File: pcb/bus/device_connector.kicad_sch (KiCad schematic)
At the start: 3 parts, among them J201 Conn_02x10_Row_Letter_First

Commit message: update bus pcb
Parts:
- removed H201, H202: MountingHole_Pad, MountingHole:MountingHole_3.2mm_M3_Pad_Via, symbol Mechanical:MountingHole_Pad
- removed J201: Conn_02x10_Row_Letter_First, PRJ:PCN10-20P-2.54DSA, symbol Connector_Generic:Conn_02x10_Row_Letter_First
- added H401, H402: MountingHole_Pad, MountingHole:MountingHole_3.2mm_M3_Pad_Via, symbol Mechanical:MountingHole_Pad
- added J701: Conn_02x10_Row_Letter_First, PRJ:PCN10-20P-2.54DSA, symbol Connector_Generic:Conn_02x10_Row_Letter_First
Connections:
- net +12V: now also J701.a10 (Pin_a10), J701.a9 (Pin_a9), J701.b10 (Pin_b10), J701.b9 (Pin_b9)
- net +5V: now also J701.a6 (Pin_a6), J701.a7 (Pin_a7), J701.b6 (Pin_b6), J701.b7 (Pin_b7)
- net GND: now also H401.1, H402.1, J701.a1 (Pin_a1), J701.a8 (Pin_a8), J701.b1 (Pin_b1), J701.b8 (Pin_b8)
- net USB+: now also J701.a5 (Pin_a5)
- net USB-: now also J701.b5 (Pin_b5)
- no-connect marks 4 -> 6
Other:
- title: Bus Connector -> (none)

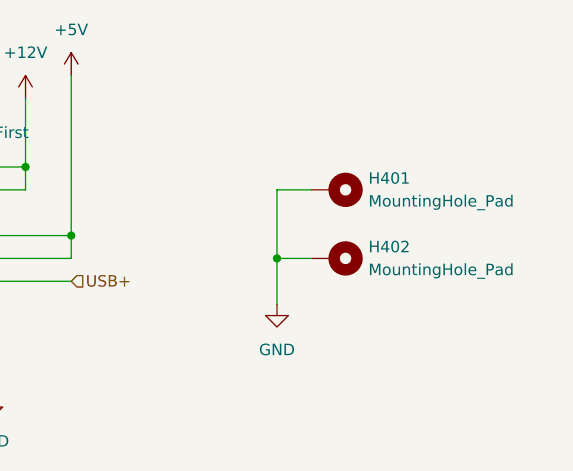
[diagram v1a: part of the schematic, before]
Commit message: update pcb size
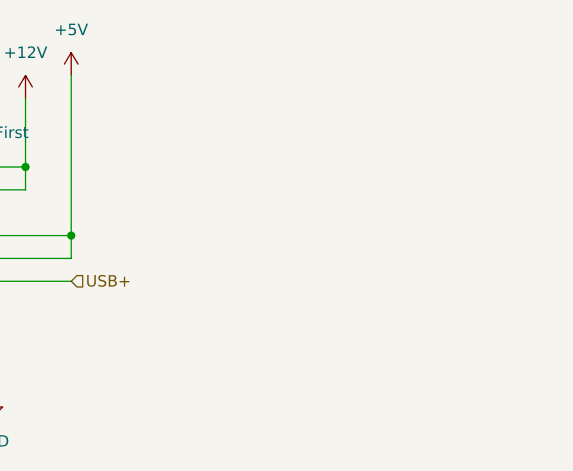
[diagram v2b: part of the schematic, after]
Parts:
- removed H401, H402: MountingHole_Pad, MountingHole:MountingHole_3.2mm_M3_Pad_Via, symbol Mechanical:MountingHole_Pad

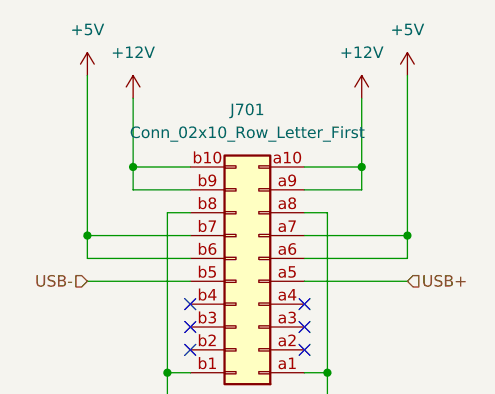
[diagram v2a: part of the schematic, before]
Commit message: upgrade to kicad 9.0.0
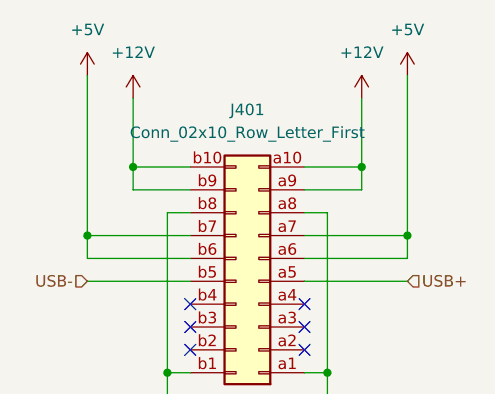
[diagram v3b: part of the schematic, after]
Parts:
- renumbered J701 to J401
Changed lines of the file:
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@@
 (kicad_sch
-	(version 20231120)
+	(version 20250114)
 	(generator "eeschema")
-	(generator_version "8.0")
+	(generator_version "9.0")
 	(paper "A4")
 	(title_block
@@
 		(dnp no)
 		(fields_autoplaced yes)
-		(property "Reference" "#PWR0705"
+		(property "Reference" "#PWR0405"
 			(at 162.56 69.85 0)
 			(effects
@@
 		(dnp no)
 		(fields_autoplaced yes)
-		(property "Reference" "#PWR0703"
+		(property "Reference" "#PWR0403"
 			(at 140.97 105.41 0)
 			(effects
@@
 		(dnp no)
 		(fields_autoplaced yes)
-		(property "Reference" "#PWR0704"
+		(property "Reference" "#PWR0404"
 			(at 158.75 105.41 0)
 			(effects
@@
 		(dnp no)
 		(fields_autoplaced yes)
-		(property "Reference" "#PWR0706"
+		(property "Reference" "#PWR0406"
 			(at 167.64 67.31 0)
 			(effects
@@
 		(dnp no)
 		(fields_autoplaced yes)
-		(property "Reference" "J701"
+		(property "Reference" "J401"
 			(at 149.86 67.31 0)
 			(effects
@@
 		(dnp no)
 		(fields_autoplaced yes)
-		(property "Reference" "#PWR0702"
+		(property "Reference" "#PWR0402"
 			(at 137.16 69.85 0)
 			(effects
@@
 		(dnp no)
 		(fields_autoplaced yes)
-		(property "Reference" "#PWR0701"
+		(property "Reference" "#PWR0401"
 			(at 132.08 67.31 0)
 			(effects

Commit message: update bus pcb
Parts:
- added C105: 100nF, Capacitor_SMD:C_0805_2012Metric, symbol Device:C
- added U103: USBLC6-2SC6, Package_TO_SOT_SMD:SOT-666, symbol Power_Protection:USBLC6-2SC6
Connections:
- net +5V: now also C105.1, U103.5 (VBUS)
- net GND: now also C105.2, U103.2 (GND)
- net USB+: now also U103.4 (I/O2); no longer J401.a5 (Pin_a5)
- net USB-: now also U103.6 (I/O1); no longer J401.b5 (Pin_b5)
- new net NS_USB+: J401.a5 (Pin_a5), U103.3 (I/O2)
- new net NS_USB-: J401.b5 (Pin_b5), U103.1 (I/O1)
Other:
- moved on the sheet: J401

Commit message: update ALL parts
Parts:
- C105: LCSC C354365 -> C28233
- J401: MOUSER (none) -> 798-PCN1020P254DSA72
- U103: LCSC (none) -> C2827654
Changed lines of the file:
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@@
 			)
 		)
-		(property "LCSC" "C354365"
+		(property "LCSC" "C28233"
 			(at 154.94 87.63 0)
 			(effects
@@
 				)
 				(hide yes)
+			)
+		)
+		(property "MOUSER" ""
+			(at 154.94 87.63 0)
+			(effects
+				(font
+					(size 1.27 1.27)
+				)
 			)
 		)
@@
 			)
 		)
+		(property "MOUSER" "798-PCN1020P254DSA72"
+			(at 90.17 91.44 0)
+			(effects
+				(font
+					(size 1.27 1.27)
+				)
+				(hide yes)
+			)
+		)
 		(pin "a3"
 		)
@@
 			)
 		)
+		(property "LCSC" "C2827654"
+			(at 201.93 85.09 0)
+			(effects
+				(font
+					(size 1.27 1.27)
+				)
+			)
+		)
+		(property "MOUSER" ""
+			(at 201.93 85.09 0)
+			(effects
+				(font
+					(size 1.27 1.27)
+				)
+			)
+		)

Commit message: fix footprint in bus pcb
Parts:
- U103: footprint Package_TO_SOT_SMD:SOT-666 -> Package_TO_SOT_SMD:SOT-23-6
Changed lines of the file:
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@@
 			)
 		)
-		(property "Footprint" "Package_TO_SOT_SMD:SOT-666"
+		(property "Footprint" "Package_TO_SOT_SMD:SOT-23-6"
 			(at 203.2 91.44 0)
 			(effects
